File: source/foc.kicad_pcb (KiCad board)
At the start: 4 copper layers, 60 x 86.7 mm, 240 parts, among them J1 Conn_01x03, J2 Conn_01x06, J3 Conn_01x08, J4 Conn_01x04_Male, J5 TYPE-C-31-M-12, P1 SWD, Q1 MMBT5401, Q10 MMBT5401, Q11 CSD19536KCS, Q12 CSD19536KCS, Q2 MMBT5401, Q3 CSD19536KCS, Q4 CSD19536KCS, Q5 MMBT5401, Q6 MMBT5401, Q7 CSD19536KCS, Q8 CSD19536KCS, Q9 MMBT5401, SW1 SW_DPDT_x2, U1 BMI160, U10 TX4130L/PW2902, U11 MS8311, U12 MS8311, U13 MS8311, U14 TJA1050T/CM,118, U15 STM32F405RGT6, U2 AMS1117-3.3, U3 MC74VHC1G66, U4 EG3112, U5 MC74VHC1G66, U6 XL1509-5.0E1, U7 EG3112, U8 MC74VHC1G66, U9 EG3112, Y1 8MHz Crystal Resonator, X5032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

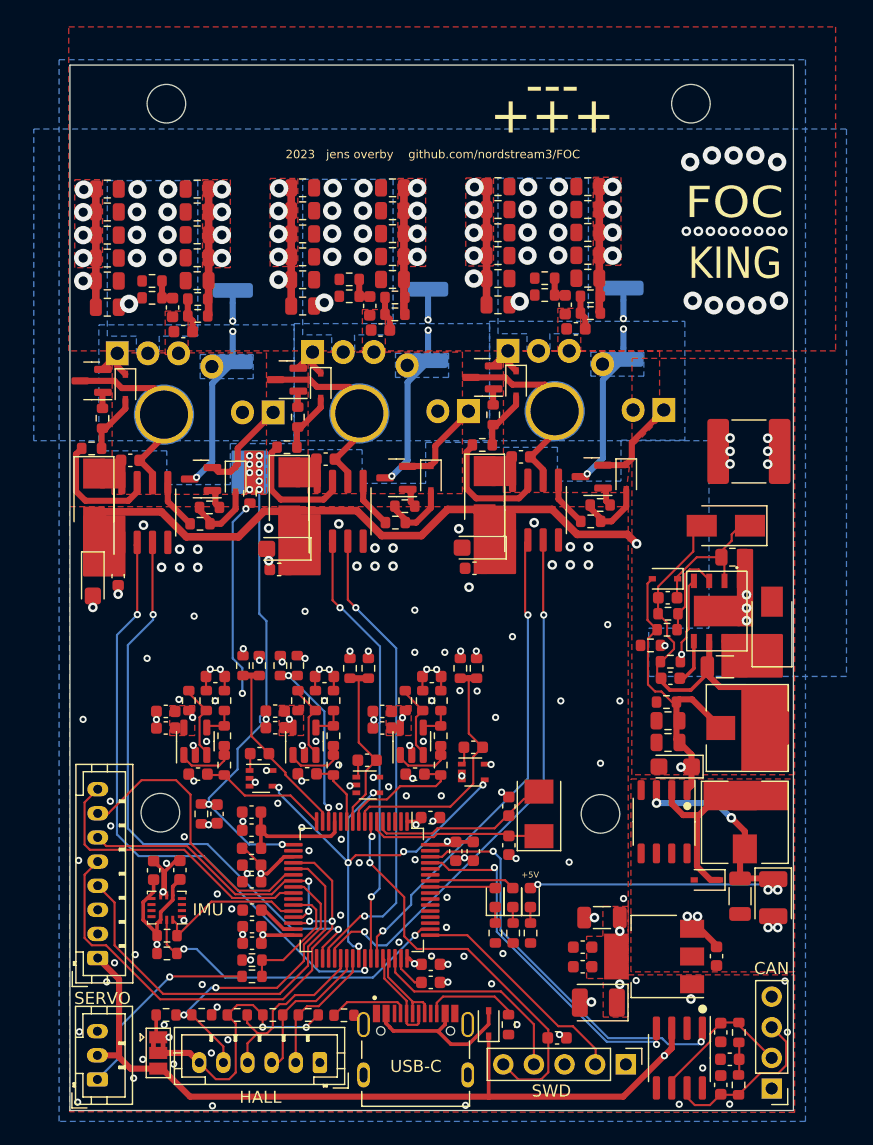
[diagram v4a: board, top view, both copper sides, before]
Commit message: Add files via upload
Filter resistor on current op-amps changed from 30k to 150R
Mosfets at 45 deg angle
Changed layout of power supply
Cut through center of board
Unnecessary components near mosfets removed
Voltage filters removed again
Crystal suspected noise source - moved to back of board
Current sensing moved to in0 - in2 (PA0-PA2)
Voltage sensing moved to in11-in13
Supply voltage moved to in10
Mosfets can now be attached to heat-sink plate using screws (that can be tightened throug holes in the board)
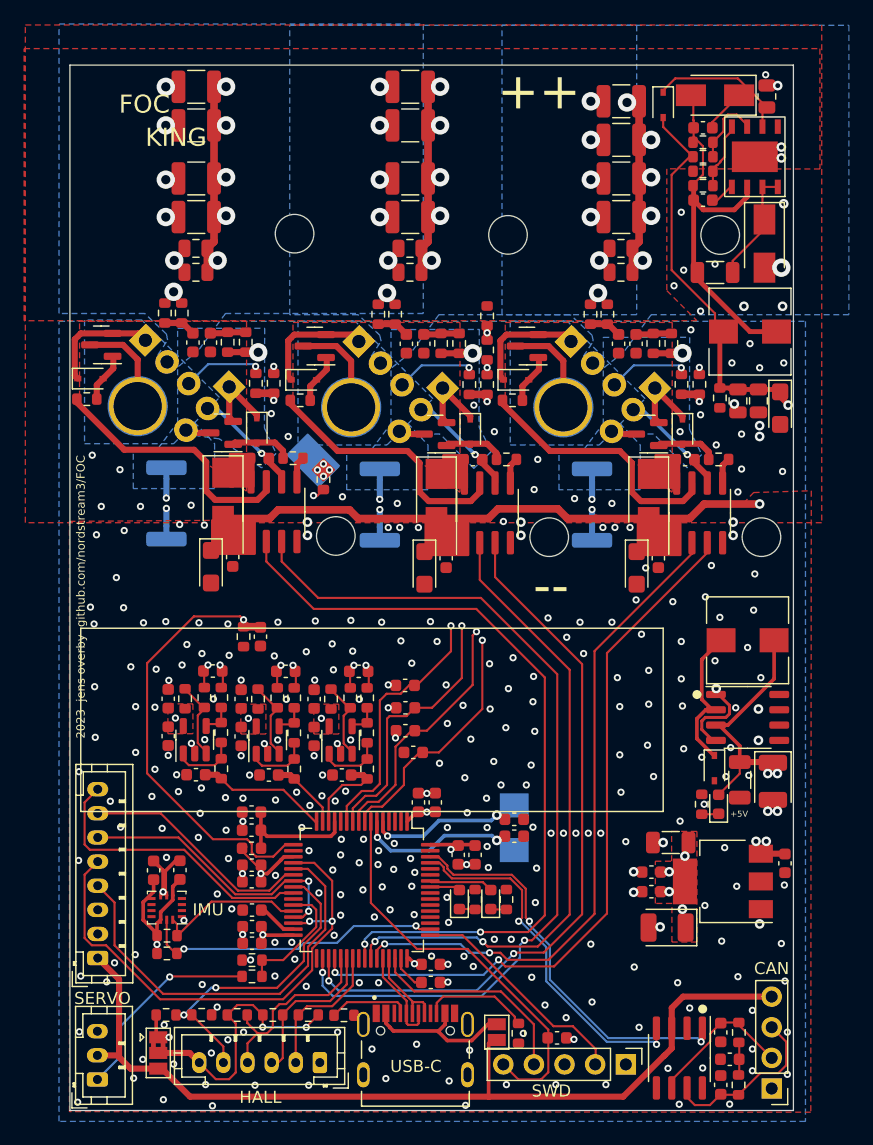
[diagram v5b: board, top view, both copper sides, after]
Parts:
- removed the C23 at (185.3, 95.3)
- removed the C25 at (166.4, 95.8)
- removed the C45 at (137.5, 83.4)
- removed the C67 at (157.6, 122.1)
- removed the C68 at (159.0, 114.0)
- removed the C69 at (164.5, 73.4)
- removed the C70 at (164.5, 75.3)
- removed the C71 at (164.5, 77.2)
- removed the C72 at (164.5, 79.1)
- removed the C73 at (164.5, 81.0)
- removed the C74 at (164.5, 83.2)
- removed the C75 at (171.9, 73.4)
- removed the C76 at (171.9, 75.3)
- removed the C77 at (171.9, 77.2)
- removed the C78 at (171.9, 79.1)
- removed the C79 at (171.9, 81.0)
- removed the C80 at (170.1, 83.2)
- removed the D15 at (163.7, 142.8)
- removed the H5 at (136.8, 92.3)
- removed the H6 at (153.0, 92.2)
- removed the R26 at (130.8, 95.1)
- removed the R27 at (139.8, 101.3)
- removed the R36 at (139.6, 84.1)
- removed the R40 at (156.8, 99.9)
- removed the R50 at (156.0, 82.6)
- removed the R61 at (159.8, 116.0)
- removed the R63 at (168.4, 81.0)
- removed the R64 at (172.2, 82.5)
- removed the R65 at (168.4, 82.4)
- removed the R66 at (172.2, 83.9)
- removed the U12 at (148.4, 119.4)
- removed U13: MS8311, Package_TO_SOT_SMD:TSOT-23-5
- removed the U4 at (135.2, 100.4)
- removed the U7 at (151.4, 100.3)
- removed the U8 at (162.4, 121.9)
- added C24: 10u, Capacitor_SMD:C_0603_1608Metric, F.Cu at (180.0, 96.0)
- added C26: 10n, Capacitor_SMD:C_0603_1608Metric, F.Cu at (157.5, 120.3)
- added C50: 4.7u 100V, Capacitor_SMD:C_1210_3225Metric, F.Cu at (157.2, 72.7)
- added H3: MountingHole, MountingHole:MountingHole_3.2mm_M3, F.Cu at (165.3, 77.4)
- added H4: MountingHole, MountingHole:MountingHole_3.2mm_M3, F.Cu at (168.8, 102.5)
- added H7: Phase_A_Pad, Custom:MountingHole_3.5mm_Pad_TopOnly_custom, B.Cu at (134.6, 91.6)
- added H8: Phase_B_Pad, Custom:MountingHole_3.5mm_Pad_TopOnly_custom, B.Cu at (152.3, 91.7)
- added R30: ASR-M-3-0.25F 0.25mR, Resistor_SMD:R_2512_6332Metric, B.Cu at (137.0, 99.6)
- added R31: 10R, Resistor_SMD:R_0603_1608Metric, F.Cu at (138.3, 83.9)
- added R38: 4.7R, Resistor_SMD:R_0603_1608Metric, F.Cu at (165.2, 96.0)
- added R44: ASR-M-3-0.25F 0.25mR, Resistor_SMD:R_2512_6332Metric, B.Cu at (154.7, 99.7)
- added SW2: SW_DPDT_x2, Jumper:SolderJumper-2_P1.3mm_Open_Pad1.0x1.5mm, F.Cu at (164.4, 143.5)
- added U10: MS8311, Package_TO_SOT_SMD:TSOT-23-5, F.Cu at (151.4, 119.3)
- added U6: EG3112, Package_SO:SOIC-8_3.9x4.9mm_P1.27mm, F.Cu at (181.2, 100.4)
- C15, C18, C9: value 100n -> 10n
- C36, C37, C38, C39, C52, C61, C62: value 100n 100V -> 4.7u 100V; footprint Capacitor_SMD:C_0805_2012Metric -> Capacitor_SMD:C_1210_3225Metric
- C40, C41, C53, C54: value 100n 100V -> 4.7n; footprint Capacitor_SMD:C_0805_2012Metric -> Capacitor_SMD:C_0603_1608Metric
- C42, C55: value 100n 100V -> 2.2u; footprint Capacitor_SMD:C_0805_2012Metric -> Capacitor_SMD:C_0603_1608Metric
- C43, C56: value 100n 100V -> 100n; footprint Capacitor_SMD:C_0805_2012Metric -> Capacitor_SMD:C_0603_1608Metric
- C44, C57: value 100n 100V -> 1n; footprint Capacitor_SMD:C_0805_2012Metric -> Capacitor_SMD:C_0603_1608Metric
- C46: value 4.7n -> 100p
- C47: value 2.2u -> 100n 100V; footprint Capacitor_SMD:C_0603_1608Metric -> Capacitor_SMD:C_0805_2012Metric
- C48: value 100n -> 100n 100V; footprint Capacitor_SMD:C_0603_1608Metric -> Capacitor_SMD:C_0805_2012Metric
- C49: value 1n -> 4.7u 100V; footprint Capacitor_SMD:C_0603_1608Metric -> Capacitor_SMD:C_1210_3225Metric
- C51: value 100p -> 4.7u 100V; footprint Capacitor_SMD:C_0603_1608Metric -> Capacitor_SMD:C_1210_3225Metric
- C58: value 100n 100V -> 100p; footprint Capacitor_SMD:C_0805_2012Metric -> Capacitor_SMD:C_0603_1608Metric
- C63, C64: value 4.7n -> 4.7u 100V; footprint Capacitor_SMD:C_0603_1608Metric -> Capacitor_SMD:C_1210_3225Metric
- C65: value 2.2u -> 4.7n
- C66: value 100n -> 4.7n
- C81: value 4.7n -> 100n
- R23: value 30k -> 150R
- R24: value 0R -> 4.7R
- R25: value 2.2R -> 4.7R
- R32, R48: value ASR-M-3-0.25F 0.25mR -> 10R; footprint Resistor_SMD:R_2512_6332Metric -> Resistor_SMD:R_0603_1608Metric; moved to F.Cu
- R35, R49: value 10R -> 150R
- R37: value 30k -> 4.7R
- R39: value 0R -> 30k
- R41: value 4.7R -> 62k
- R42, R55: value 2.2R -> 1k
- R43: value 30k -> 1k
- R45, R59: value 62k -> 10R
- R46, R47, R60: value 1k -> 10R
- R51: value 10R -> 4.7R
- R52: value 10R -> 30k
- R53: value 30k -> 62k
- R54: value 0R -> 1k
- R57: value 2.2R -> 10R
- R58: value 30k -> 10R
- U3, U5: value MC74VHC1G66 -> EG3112; footprint Package_TO_SOT_SMD:SOT-353_SC-70-5 -> Package_SO:SOIC-8_3.9x4.9mm_P1.27mm
- U9: value EG3112 -> MS8311; footprint Package_SO:SOIC-8_3.9x4.9mm_P1.27mm -> Package_TO_SOT_SMD:TSOT-23-5
- Y1: moved to B.Cu
- moved H5 66.7 mm to (182.9, 77.4)
- moved C44 49.0 mm to (145.5, 122.2)
- moved C49 47.0 mm to (157.2, 75.9)
- moved H2 46.4 mm to (151.1, 102.3)
- moved C51 46.3 mm to (157.2, 68.3), turned to 0 degrees
- moved C43 43.7 mm to (143.2, 119.0), turned to 90 degrees
- moved C81 41.4 mm to (157.9, 124.5), turned to 90 degrees
- moved C48 41.3 mm to (157.2, 78.5)
- moved R35 40.8 mm to (147.6, 121.7), turned to -90 degrees
- moved R49 40.6 mm to (153.7, 121.7), turned to -90 degrees
- moved C58 40.2 mm to (152.9, 113.6), turned to 180 degrees
- moved C25 39.7 mm to (181.5, 74.5)
- moved R18 39.6 mm to (181.5, 73.3)
- moved R17 39.6 mm to (181.5, 72.1)
- moved R16 39.3 mm to (181.5, 70.9)
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- renumbered C24 to C23, C26 to C25, C50 to C45, C82 to C67, C83 to C68, C84 to C69, C85 to C70, C86 to C71, C87 to C72, C88 to C73, C89 to C74, C90 to C75, C91 to C76, C92 to C77, C93 to C78, C94 to C79, C95 to C80, C96 to C82, C97 to C83, C98 to C84, C99 to C85, D16 to D15, D17 to D16, H3 to H5, H4 to H6, H7 to H9, R28 to R26, R29 to R27, R30 to R28, R31 to R29, R38 to R36, R44 to R40, R56 to R50, R62 to R56, R67 to R61, R68 to R62, R69 to R63, R70 to R64, R71 to R65, R72 to R66, R73 to R67, U14 to U11, U15 to U12, U6 to U4, U10 to U7, U11 to U8
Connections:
- C15 pad 2: Net-(C15-Pad2) -> GND
- C18 pad 2: Net-(C18-Pad2) -> GND
- C40 pad 1: V_IN -> /driver/HS1
- C40 pad 2: GND -> Net-(C40-Pad2)
- C41 pad 1: V_IN -> /driver/HS1
- C41 pad 2: GND -> Net-(C41-Pad2)
- C42 pad 1: V_IN -> GND
- C42 pad 2: GND -> VCC
- C43 pad 1: V_IN -> GND
- C43 pad 2: GND -> VCC
- C44 pad 1: V_IN -> GND
- C44 pad 2: GND -> /mcu/CURRENT_2
- C46 pad 1: /driver/HS1 -> Net-(C46-Pad1)
- C47 pad 1: GND -> V_IN
- C47 pad 2: VCC -> GND
- C48 pad 1: GND -> V_IN
- C48 pad 2: VCC -> GND
- C49 pad 1: GND -> V_IN
- C49 pad 2: /mcu/CURRENT_2 -> GND
- C51 pad 1: Net-(C51-Pad1) -> V_IN
- C51 pad 2: Net-(C51-Pad2) -> GND
- C53 pad 1: V_IN -> /driver/HS2
- C53 pad 2: GND -> Net-(C53-Pad2)
- C54 pad 1: V_IN -> /driver/HS2
- C54 pad 2: GND -> Net-(C54-Pad2)
- C55 pad 1: V_IN -> VCC
- C56 pad 1: V_IN -> VCC
- C57 pad 1: V_IN -> GND
- C57 pad 2: GND -> /mcu/CURRENT_3
- C58 pad 1: V_IN -> Net-(C58-Pad1)
- C58 pad 2: GND -> Net-(C58-Pad2)
- C63 pad 1: /driver/HS2 -> V_IN
- C63 pad 2: Net-(C63-Pad2) -> GND
- C64 pad 1: /driver/HS2 -> V_IN
- C64 pad 2: Net-(C64-Pad2) -> GND
- C65 pad 1: VCC -> /driver/HS3
- C65 pad 2: GND -> Net-(C65-Pad2)
- C66 pad 1: VCC -> /driver/HS3
- C66 pad 2: GND -> Net-(C66-Pad2)
- C81 pad 1: /driver/HS3 -> VCC
- C81 pad 2: Net-(C81-Pad2) -> GND
- C9 pad 2: Net-(C9-Pad2) -> GND
- D6 pad 1: Net-(C25-Pad1) -> Net-(C24-Pad1)
- NT3 pad 1: Net-(C51-Pad2) -> Net-(C46-Pad2)
- NT4 pad 1: Net-(C51-Pad1) -> Net-(C46-Pad1)
- NT5 pad 1: Net-(C68-Pad2) -> Net-(C58-Pad2)
- NT6 pad 1: Net-(C68-Pad1) (its old number) -> Net-(C58-Pad1)
- Q1 pad 1: Net-(Q1-Pad1) -> Net-(D8-Pad2)
- Q10 pad 1: Net-(Q10-Pad1) -> Net-(D13-Pad2)
- Q2 pad 1: Net-(Q2-Pad1) -> Net-(D9-Pad2)
- Q5 pad 1: Net-(Q5-Pad1) -> Net-(D10-Pad2)
- Q6 pad 1: Net-(Q6-Pad1) -> Net-(D11-Pad2)
- Q9 pad 1: Net-(Q9-Pad1) -> Net-(D12-Pad2)
- R24 pad 1: Net-(Q1-Pad1) -> /driver/HO1
- R25 pad 1: Net-(Q2-Pad1) -> /driver/LO1
- R32 pad 1: Net-(NT1-Pad2) -> Net-(C41-Pad2)
- R33 pad 1: Net-(C45-Pad2) -> Net-(C40-Pad2)
- R34 pad 1: Net-(C46-Pad2) -> Net-(C41-Pad2)
- R35 pad 1: Net-(C45-Pad2) -> Net-(R35-Pad1)
- R35 pad 2: V_IN -> /mcu/CURRENT_2
- R37 pad 1: Net-(R37-Pad1) -> /driver/HO2
- R37 pad 2: /mcu/CURRENT_2 -> Net-(D10-Pad2)
- R39 pad 1: Net-(Q5-Pad1) -> Net-(R39-Pad1)
- R39 pad 2: Net-(D10-Pad2) -> Net-(R35-Pad1)
- R41 pad 1: /driver/HO2 -> Net-(R41-Pad1)
- R41 pad 2: Net-(D10-Pad2) -> VCC
- R42 pad 1: /driver/LO2 -> Net-(C46-Pad2)
- R42 pad 2: Net-(D11-Pad2) -> Net-(R41-Pad1)
- R43 pad 1: Net-(R43-Pad1) -> Net-(C46-Pad1)
- R43 pad 2: Net-(R37-Pad1) -> Net-(R39-Pad1)
- R45 pad 1: Net-(R45-Pad1) -> Net-(C53-Pad2)
- R45 pad 2: VCC -> V_IN
- R46 pad 1: Net-(C51-Pad2) -> Net-(C54-Pad2)
- R46 pad 2: Net-(R45-Pad1) -> GND
- R47 pad 1: Net-(C51-Pad1) -> Net-(C53-Pad2)
- R47 pad 2: Net-(R43-Pad1) -> V_IN
- R48 pad 1: Net-(NT3-Pad2) -> Net-(C54-Pad2)
- R49 pad 1: Net-(C63-Pad2) -> Net-(R49-Pad1)
- R49 pad 2: V_IN -> /mcu/CURRENT_3
- R51 pad 1: Net-(C63-Pad2) -> /driver/LO3
- R51 pad 2: V_IN -> Net-(D13-Pad2)
- R52 pad 1: Net-(C64-Pad2) -> Net-(R52-Pad1)
- R52 pad 2: GND -> Net-(R49-Pad1)
- R53 pad 2: /mcu/CURRENT_3 -> VCC
- R54 pad 1: Net-(Q9-Pad1) -> Net-(C58-Pad2)
- R54 pad 2: Net-(D12-Pad2) -> Net-(R53-Pad1)
- R55 pad 1: Net-(Q10-Pad1) -> Net-(C58-Pad1)
- R55 pad 2: Net-(D13-Pad2) -> Net-(R52-Pad1)
- R57 pad 1: /driver/LO3 -> Net-(C65-Pad2)
- R57 pad 2: Net-(D13-Pad2) -> V_IN
- R58 pad 1: Net-(R58-Pad1) -> Net-(C66-Pad2)
- R58 pad 2: Net-(R53-Pad1) -> GND
- R59 pad 1: Net-(R59-Pad1) -> Net-(C65-Pad2)
- R59 pad 2: VCC -> V_IN
- R60 pad 1: Net-(C68-Pad2) -> Net-(C66-Pad2)
- R60 pad 2: Net-(R59-Pad1) -> GND
- U12 pad 11: /mcu/CURRENT_2 -> /driver/SENS_1
- U12 pad 14: /driver/SENS_SUPPLY -> /mcu/CURRENT_3
- U12 pad 15: /driver/SENS_1 -> /mcu/CURRENT_2
- U12 pad 40: /driver/SENS_FILTER -> unconnected-(U12-Pad40)
- U12 pad 8: /driver/SENS_3 -> /driver/SENS_SUPPLY
- U12 pad 9: /mcu/CURRENT_3 -> /driver/SENS_3
- U3 pad 1: Net-(C9-Pad2) -> +12V
- U3 pad 2: GND -> /driver/H1
- U3 pad 3: GND -> /driver/L1
- U3 pad 4: /driver/SENS_FILTER -> GND
- U3 pad 5: VCC -> /driver/LO1
- U5 pad 1: Net-(C15-Pad2) -> +12V
- U5 pad 2: GND -> /driver/H2
- U5 pad 3: GND -> /driver/L2
- U5 pad 4: /driver/SENS_FILTER -> GND
- U5 pad 5: VCC -> /driver/LO2
- U9 pad 1: +12V -> Net-(R35-Pad1)
- U9 pad 2: /driver/H3 -> GND
- U9 pad 3: /driver/L3 -> Net-(R41-Pad1)
- U9 pad 4: GND -> Net-(R39-Pad1)
- U9 pad 5: /driver/LO3 -> VCC
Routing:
- net Net-(C68-Pad1) (its old number): track 39.6 -> 0.00 mm, vias 2 -> 0
- net Net-(C68-Pad2): track 39.1 -> 0.00 mm, vias 2 -> 0
- net /driver/SENS_FILTER: track 37.2 -> 0.00 mm, vias 6 -> 0
- net Net-(C51-Pad1): track 36.6 -> 0.00 mm, vias 2 -> 0
- net /driver/SENS_SUPPLY: track 13.5 -> 49.7 mm
- net Net-(C51-Pad2): track 36.1 -> 0.00 mm, vias 2 -> 0
- net /driver/SENS_1: track 16.1 -> 50.1 mm, vias 0 -> 2
- net /driver/SENS_3: track 21.7 -> 54.2 mm, vias 0 -> 2
- net Net-(C58-Pad2): track 0.00 -> 31.3 mm, vias 0 -> 2
- net Net-(C58-Pad1): track 0.00 -> 30.7 mm, vias 0 -> 2
- net /driver/SENS_2: track 14.5 -> 44.0 mm, vias 0 -> 2
- net V_IN: track 28.0 -> 0.00 mm, vias 53 -> 22
- net /driver/L1: track 48.5 -> 73.8 mm
- net Net-(C46-Pad1): track 0.00 -> 21.9 mm, vias 0 -> 2
- net /driver/HS3: track 45.5 -> 23.9 mm, vias 1 -> 2
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- added copper zone on B.Cu, net /driver/HS1
- added copper zone on B.Cu, net /driver/HS2
- added copper zone on B.Cu, net /driver/HS3
- removed copper zone on In2.Cu, net V_IN
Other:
- board text added: "++"
- board text added: "++ Solder to corner of heatsink"
- board text added: "--"
- board text removed: "+++"
- board text removed: "---"
